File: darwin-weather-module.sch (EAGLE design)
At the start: 22 parts, among them J1 2X6-HEADERS, J2 95501-6889VERT, U2 ATSAMD09, U3 M24C02-WMN6TP, U4 PCA9615

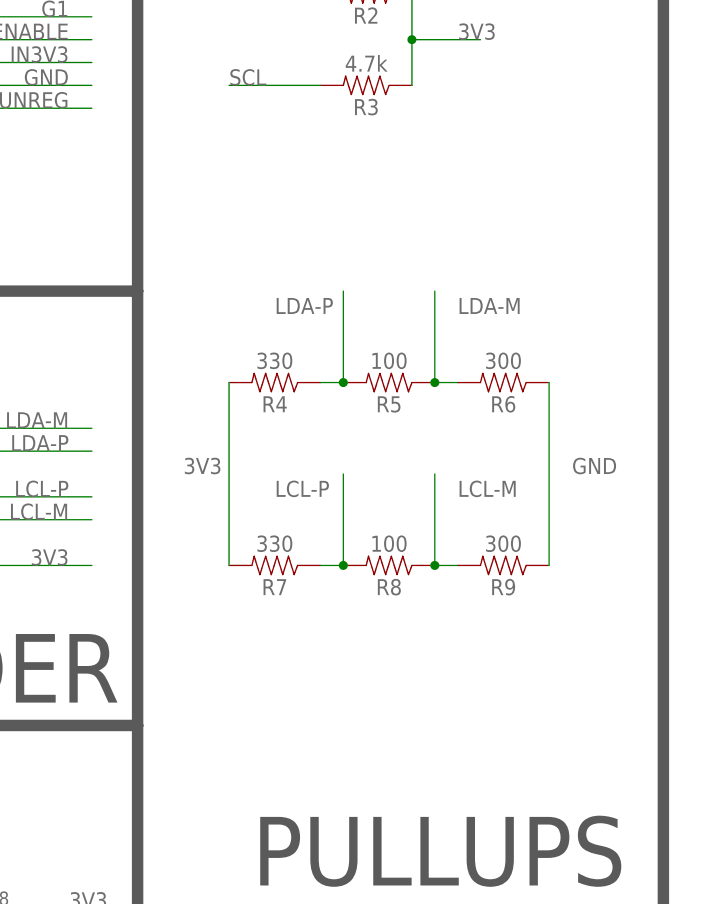
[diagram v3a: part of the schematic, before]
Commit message: Fixed pullups and mfg cleanup.
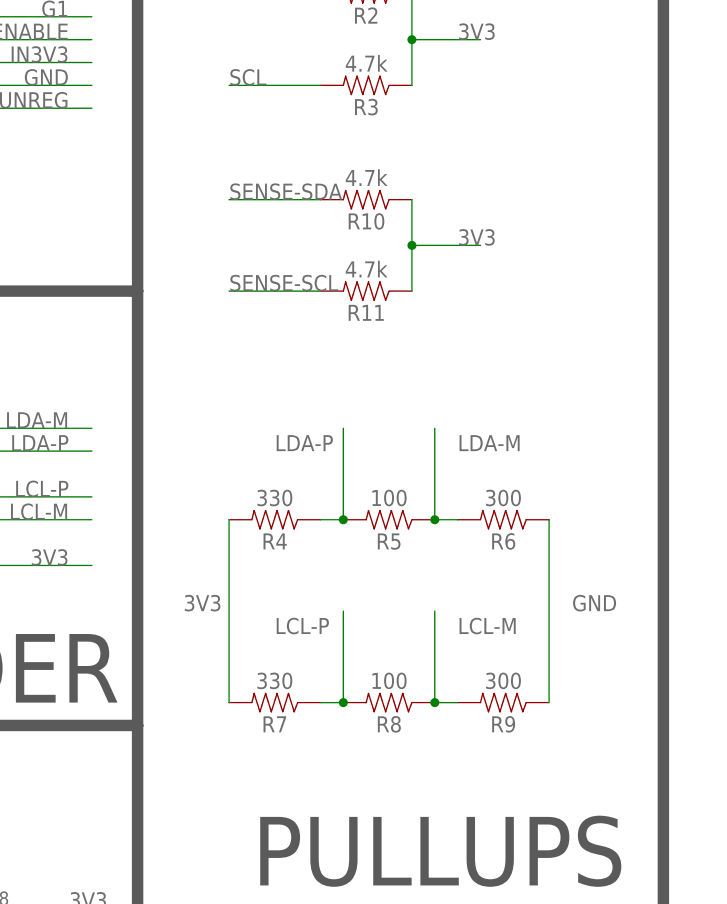
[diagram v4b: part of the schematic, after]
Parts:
- added R10, R11: 4.7k, SparkFun-Resistors:100KOHM-0603-1/10W-1%
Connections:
- net 3V3: now also R10.1, R11.1
- net SENSE-SCL: now also R11.2
- net SENSE-SDA: now also R10.2
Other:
- moved on the sheet: R4, R5, R6, R7, R8, R9
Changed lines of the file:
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@@
 <?xml version="1.0" encoding="utf-8"?>
 <!DOCTYPE eagle SYSTEM "eagle.dtd">
-<eagle version="9.4.2">
+<eagle version="9.5.0">
 <drawing>
 <settings>
@@
 <part name="R8" library="SparkFun-Resistors" library_urn="urn:adsk.eagle:library:532" deviceset="100KOHM" device="-0603-1/10W-1%" package3d_urn="urn:adsk.eagle:package:39650/1" value="100"/>
 <part name="R9" library="SparkFun-Resistors" library_urn="urn:adsk.eagle:library:532" deviceset="100KOHM" device="-0603-1/10W-1%" package3d_urn="urn:adsk.eagle:package:39650/1" value="300"/>
+<part name="R10" library="SparkFun-Resistors" library_urn="urn:adsk.eagle:library:532" deviceset="100KOHM" device="-0603-1/10W-1%" package3d_urn="urn:adsk.eagle:package:39650/1" value="4.7k"/>
+<part name="R11" library="SparkFun-Resistors" library_urn="urn:adsk.eagle:library:532" deviceset="100KOHM" device="-0603-1/10W-1%" package3d_urn="urn:adsk.eagle:package:39650/1" value="4.7k"/>
 </parts>
 <sheets>
@@
 <attribute name="NAME" x="139.446" y="59.436" size="1.778" layer="94"/>
 </instance>
-<instance part="R4" gate="G$1" x="208.28" y="53.34" smashed="yes" rot="R180">
-<attribute name="NAME" x="208.28" y="51.816" size="1.778" layer="95" font="vector" rot="R180" align="bottom-center"/>
-<attribute name="VALUE" x="208.28" y="54.864" size="1.778" layer="96" font="vector" rot="R180" align="top-center"/>
-</instance>
-<instance part="R5" gate="G$1" x="220.98" y="53.34" smashed="yes" rot="R180">
-<attribute name="NAME" x="220.98" y="51.816" size="1.778" layer="95" font="vector" rot="R180" align="bottom-center"/>
-<attribute name="VALUE" x="220.98" y="54.864" size="1.778" layer="96" font="vector" rot="R180" align="top-center"/>
-</instance>
-<instance part="R6" gate="G$1" x="233.68" y="53.34" smashed="yes" rot="R180">
-<attribute name="NAME" x="233.68" y="51.816" size="1.778" layer="95" font="vector" rot="R180" align="bottom-center"/>
-<attribute name="VALUE" x="233.68" y="54.864" size="1.778" layer="96" font="vector" rot="R180" align="top-center"/>
-</instance>
-<instance part="R7" gate="G$1" x="208.28" y="33.02" smashed="yes" rot="R180">
-<attribute name="NAME" x="208.28" y="31.496" size="1.778" layer="95" font="vector" rot="R180" align="bottom-center"/>
-<attribute name="VALUE" x="208.28" y="34.544" size="1.778" layer="96" font="vector" rot="R180" align="top-center"/>
-</instance>
-<instance part="R8" gate="G$1" x="220.98" y="33.02" smashed="yes" rot="R180">
-<attribute name="NAME" x="220.98" y="31.496" size="1.778" layer="95" font="vector" rot="R180" align="bottom-center"/>
-<attribute name="VALUE" x="220.98" y="34.544" size="1.778" layer="96" font="vector" rot="R180" align="top-center"/>
-</instance>
-<instance part="R9" gate="G$1" x="233.68" y="33.02" smashed="yes" rot="R180">
-<attribute name="NAME" x="233.68" y="31.496" size="1.778" layer="95" font="vector" rot="R180" align="bottom-center"/>
-<attribute name="VALUE" x="233.68" y="34.544" size="1.778" layer="96" font="vector" rot="R180" align="top-center"/>
+<instance part="R4" gate="G$1" x="208.28" y="38.1" smashed="yes" rot="R180">
+<attribute name="NAME" x="208.28" y="36.576" size="1.778" layer="95" font="vector" rot="R180" align="bottom-center"/>
+<attribute name="VALUE" x="208.28" y="39.624" size="1.778" layer="96" font="vector" rot="R180" align="top-center"/>
+</instance>
+<instance part="R5" gate="G$1" x="220.98" y="38.1" smashed="yes" rot="R180">
+<attribute name="NAME" x="220.98" y="36.576" size="1.778" layer="95" font="vector" rot="R180" align="bottom-center"/>
+<attribute name="VALUE" x="220.98" y="39.624" size="1.778" layer="96" font="vector" rot="R180" align="top-center"/>
+</instance>
+<instance part="R6" gate="G$1" x="233.68" y="38.1" smashed="yes" rot="R180">
+<attribute name="NAME" x="233.68" y="36.576" size="1.778" layer="95" font="vector" rot="R180" align="bottom-center"/>
+<attribute name="VALUE" x="233.68" y="39.624" size="1.778" layer="96" font="vector" rot="R180" align="top-center"/>
+</instance>
+<instance part="R7" gate="G$1" x="208.28" y="17.78" smashed="yes" rot="R180">
+<attribute name="NAME" x="208.28" y="16.256" size="1.778" layer="95" font="vector" rot="R180" align="bottom-center"/>
+<attribute name="VALUE" x="208.28" y="19.304" size="1.778" layer="96" font="vector" rot="R180" align="top-center"/>
+</instance>
+<instance part="R8" gate="G$1" x="220.98" y="17.78" smashed="yes" rot="R180">
+<attribute name="NAME" x="220.98" y="16.256" size="1.778" layer="95" font="vector" rot="R180" align="bottom-center"/>
+<attribute name="VALUE" x="220.98" y="19.304" size="1.778" layer="96" font="vector" rot="R180" align="top-center"/>
+</instance>
+<instance part="R9" gate="G$1" x="233.68" y="17.78" smashed="yes" rot="R180">
+<attribute name="NAME" x="233.68" y="16.256" size="1.778" layer="95" font="vector" rot="R180" align="bottom-center"/>
+<attribute name="VALUE" x="233.68" y="19.304" size="1.778" layer="96" font="vector" rot="R180" align="top-center"/>
+</instance>
+<instance part="R10" gate="G$1" x="218.44" y="73.66" smashed="yes" rot="R180">
+<attribute name="NAME" x="218.44" y="72.136" size="1.778" layer="95" font="vector" rot="R180" align="bottom-center"/>
+<attribute name="VALUE" x="218.44" y="75.184" size="1.778" layer="96" font="vector" rot="R180" align="top-center"/>
+</instance>
+<instance part="R11" gate="G$1" x="218.44" y="63.5" smashed="yes" rot="R180">
+<attribute name="NAME" x="218.44" y="61.976" size="1.778" layer="95" font="vector" rot="R180" align="bottom-center"/>
+<attribute name="VALUE" x="218.44" y="65.024" size="1.778" layer="96" font="vector" rot="R180" align="top-center"/>
 </instance>
 </instances>
@@
 <pinref part="R6" gate="G$1" pin="1"/>
 <pinref part="R9" gate="G$1" pin="1"/>
-<wire x1="238.76" y1="53.34" x2="238.76" y2="33.02" width="0.1524" layer="91"/>
-<label x="241.3" y="43.18" size="1.778" layer="95"/>
+<wire x1="238.76" y1="38.1" x2="238.76" y2="17.78" width="0.1524" layer="91"/>
+<label x="241.3" y="27.94" size="1.778" layer="95"/>
 </segment>
 </net>
@@
 <pinref part="R4" gate="G$1" pin="2"/>
 <pinref part="R7" gate="G$1" pin="2"/>
-<wire x1="203.2" y1="53.34" x2="203.2" y2="33.02" width="0.1524" layer="91"/>
-<label x="198.12" y="43.18" size="1.778" layer="95"/>
+<wire x1="203.2" y1="38.1" x2="203.2" y2="17.78" width="0.1524" layer="91"/>
+<label x="198.12" y="27.94" size="1.778" layer="95"/>
+</segment>
+<segment>
+<pinref part="R11" gate="G$1" pin="1"/>
+<pinref part="R10" gate="G$1" pin="1"/>
+<wire x1="223.52" y1="63.5" x2="223.52" y2="68.58" width="0.1524" layer="91"/>
+<wire x1="223.52" y1="68.58" x2="223.52" y2="73.66" width="0.1524" layer="91"/>
+<wire x1="223.52" y1="68.58" x2="231.14" y2="68.58" width="0.1524" layer="91"/>
+<junction x="223.52" y="68.58"/>
+<label x="228.6" y="68.58" size="1.778" layer="95"/>
 </segment>
 </net>
@@
 <label x="124.46" y="45.72" size="1.778" layer="95"/>
 </segment>
+<segment>
+<pinref part="R10" gate="G$1" pin="2"/>
+<wire x1="213.36" y1="73.66" x2="203.2" y2="73.66" width="0.1524" layer="91"/>
+<label x="203.2" y="73.66" size="1.778" layer="95"/>
+</segment>
 </net>
 <net name="SENSE-SCL" class="0">
@@
 <wire x1="134.62" y1="40.64" x2="121.92" y2="40.64" width="0.1524" layer="91"/>
 <label x="124.46" y="40.64" size="1.778" layer="95"/>
+</segment>
+<segment>
+<pinref part="R11" gate="G$1" pin="2"/>
+<wire x1="213.36" y1="63.5" x2="203.2" y2="63.5" width="0.1524" layer="91"/>
+<label x="203.2" y="63.5" size="1.778" layer="95"/>
 </segment>
 </net>
@@
 <pinref part="R9" gate="G$1" pin="2"/>
 <pinref part="R8" gate="G$1" pin="1"/>
-<wire x1="228.6" y1="33.02" x2="226.06" y2="33.02" width="0.1524" layer="91"/>
-<wire x1="226.06" y1="33.02" x2="226.06" y2="43.18" width="0.1524" layer="91"/>
-<junction x="226.06" y="33.02"/>
-<label x="228.6" y="40.64" size="1.778" layer="95"/>
+<wire x1="228.6" y1="17.78" x2="226.06" y2="17.78" width="0.1524" layer="91"/>
+<wire x1="226.06" y1="17.78" x2="226.06" y2="27.94" width="0.1524" layer="91"/>
+<junction x="226.06" y="17.78"/>
+<label x="228.6" y="25.4" size="1.778" layer="95"/>
 </segment>
 </net>
@@
 <pinref part="R7" gate="G$1" pin="1"/>
 <pinref part="R8" gate="G$1" pin="2"/>
-<wire x1="213.36" y1="33.02" x2="215.9" y2="33.02" width="0.1524" layer="91"/>
-<wire x1="215.9" y1="33.02" x2="215.9" y2="43.18" width="0.1524" layer="91"/>
-<junction x="215.9" y="33.02"/>
-<label x="208.28" y="40.64" size="1.778" layer="95"/>
+<wire x1="213.36" y1="17.78" x2="215.9" y2="17.78" width="0.1524" layer="91"/>
+<wire x1="215.9" y1="17.78" x2="215.9" y2="27.94" width="0.1524" layer="91"/>
+<junction x="215.9" y="17.78"/>
+<label x="208.28" y="25.4" size="1.778" layer="95"/>
 </segment>
 </net>
@@
 <pinref part="R4" gate="G$1" pin="1"/>
 <pinref part="R5" gate="G$1" pin="2"/>
-<wire x1="213.36" y1="53.34" x2="215.9" y2="53.34" width="0.1524" layer="91"/>
-<wire x1="215.9" y1="53.34" x2="215.9" y2="63.5" width="0.1524" layer="91"/>
-<junction x="215.9" y="53.34"/>
-<label x="208.28" y="60.96" size="1.778" layer="95"/>
+<wire x1="213.36" y1="38.1" x2="215.9" y2="38.1" width="0.1524" layer="91"/>
+<wire x1="215.9" y1="38.1" x2="215.9" y2="48.26" width="0.1524" layer="91"/>
+<junction x="215.9" y="38.1"/>
+<label x="208.28" y="45.72" size="1.778" layer="95"/>
 </segment>
 </net>
@@
 <pinref part="R6" gate="G$1" pin="2"/>
 <pinref part="R5" gate="G$1" pin="1"/>
-<wire x1="228.6" y1="53.34" x2="226.06" y2="53.34" width="0.1524" layer="91"/>
-<wire x1="226.06" y1="53.34" x2="226.06" y2="63.5" width="0.1524" layer="91"/>
-<junction x="226.06" y="53.34"/>
-<label x="228.6" y="60.96" size="1.778" layer="95"/>
-</segment>
-</net>
+<wire x1="228.6" y1="38.1" x2="226.06" y2="38.1" width="0.1524" layer="91"/>
+<wire x1="226.06" y1="38.1" x2="226.06" y2="48.26" width="0.1524" layer="91"/>
+<junction x="226.06" y="38.1"/>
+<label x="228.6" y="45.72" size="1.778" layer="95"/>
+</segment>
+</net>

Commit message: Changed Power Architecture for Sensor/Module synchronization. TA3.
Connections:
- net ENABLE: now also J2.P3
- net UNREG: no longer J2.P3
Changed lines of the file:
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@@
 <segment>
 <pinref part="J2" gate="G$1" pin="P4"/>
-<pinref part="J2" gate="G$1" pin="P3"/>
-<wire x1="55.88" y1="91.44" x2="55.88" y2="93.98" width="0.1524" layer="91"/>
-<wire x1="55.88" y1="93.98" x2="63.5" y2="93.98" width="0.1524" layer="91"/>
-<junction x="55.88" y="93.98"/>
+<wire x1="55.88" y1="91.44" x2="63.5" y2="91.44" width="0.1524" layer="91"/>
 <label x="58.42" y="91.44" size="1.778" layer="95"/>
 </segment>
@@
 <label x="45.72" y="2.54" size="1.778" layer="95"/>
 </segment>
-</net>
+<segment>
+<pinref part="J2" gate="G$1" pin="P3"/>
+<wire x1="55.88" y1="93.98" x2="63.5" y2="93.98" width="0.1524" layer="91"/>
+<label x="58.42" y="93.98" size="1.778" layer="95"/>
+</segment>
+</net>
